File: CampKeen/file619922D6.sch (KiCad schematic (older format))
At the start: 40 parts

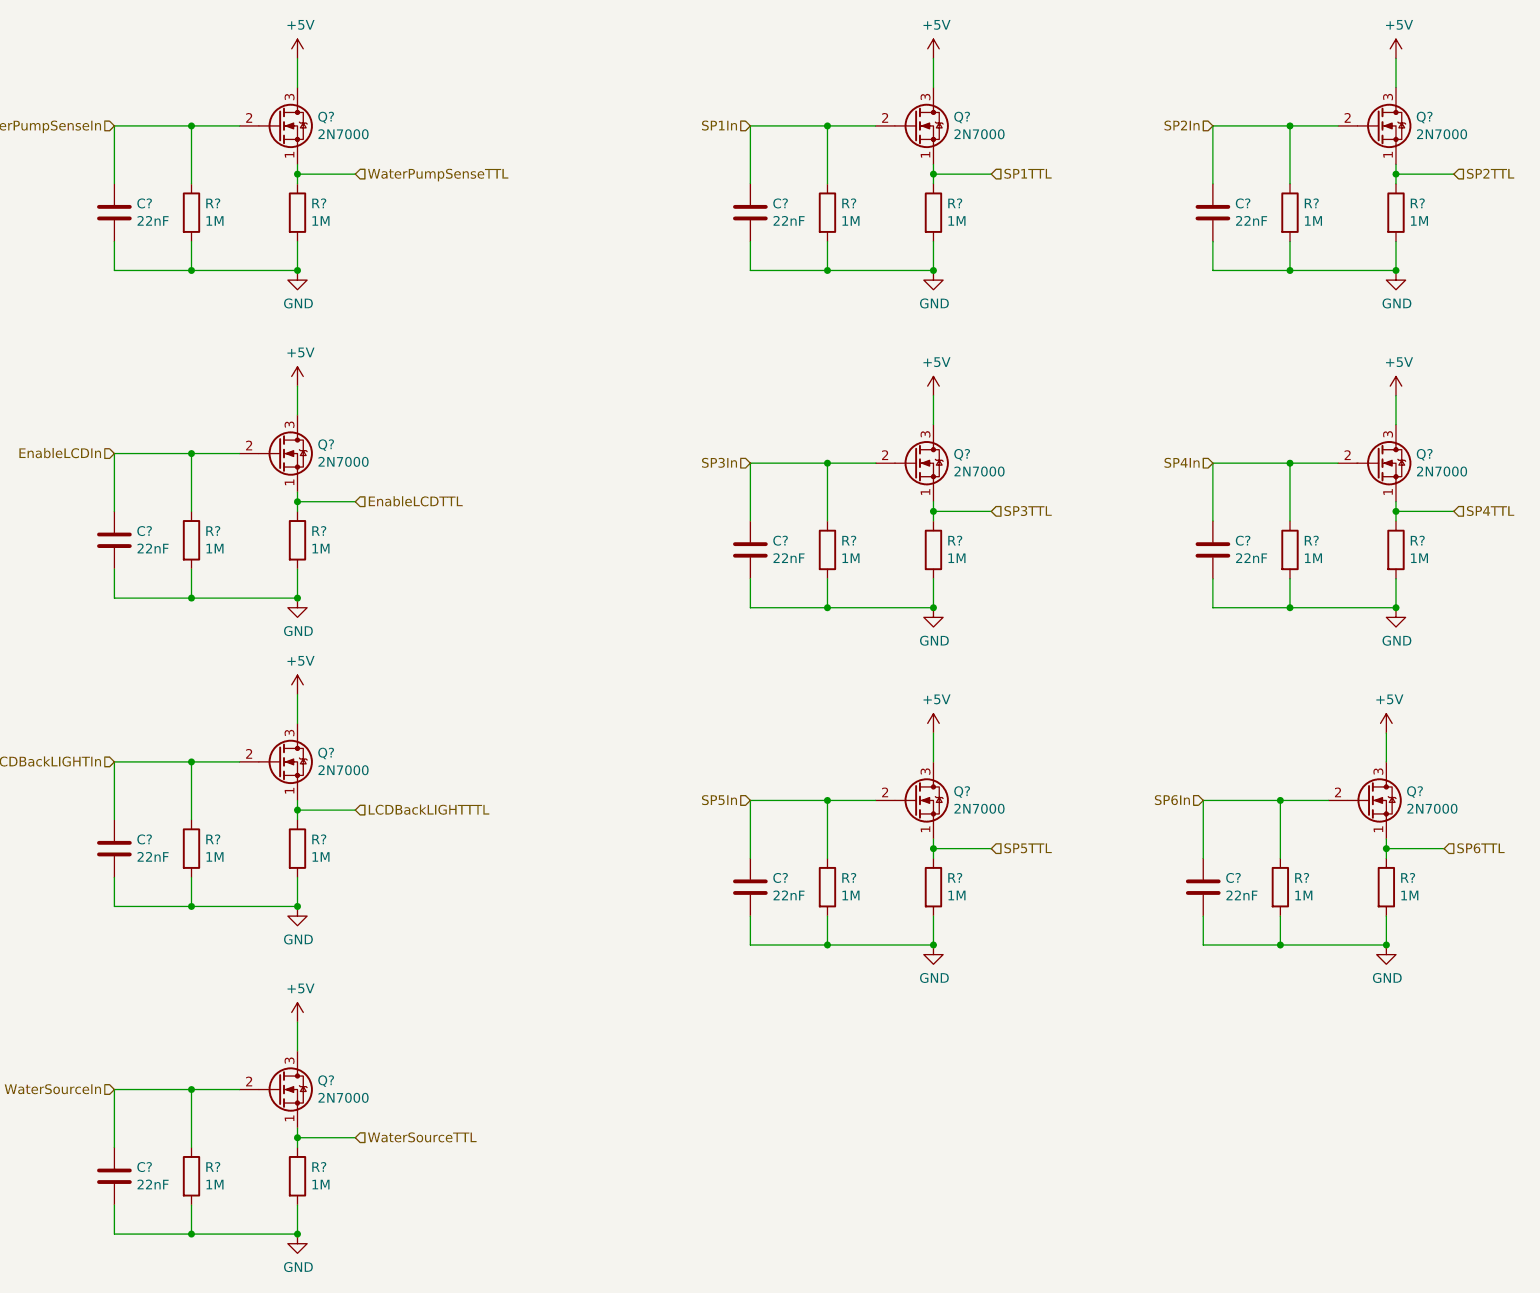
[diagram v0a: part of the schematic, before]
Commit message: updated the pin mapping to the terms. cleaned up the Schematic. PCB placement and routing is what is left to do.
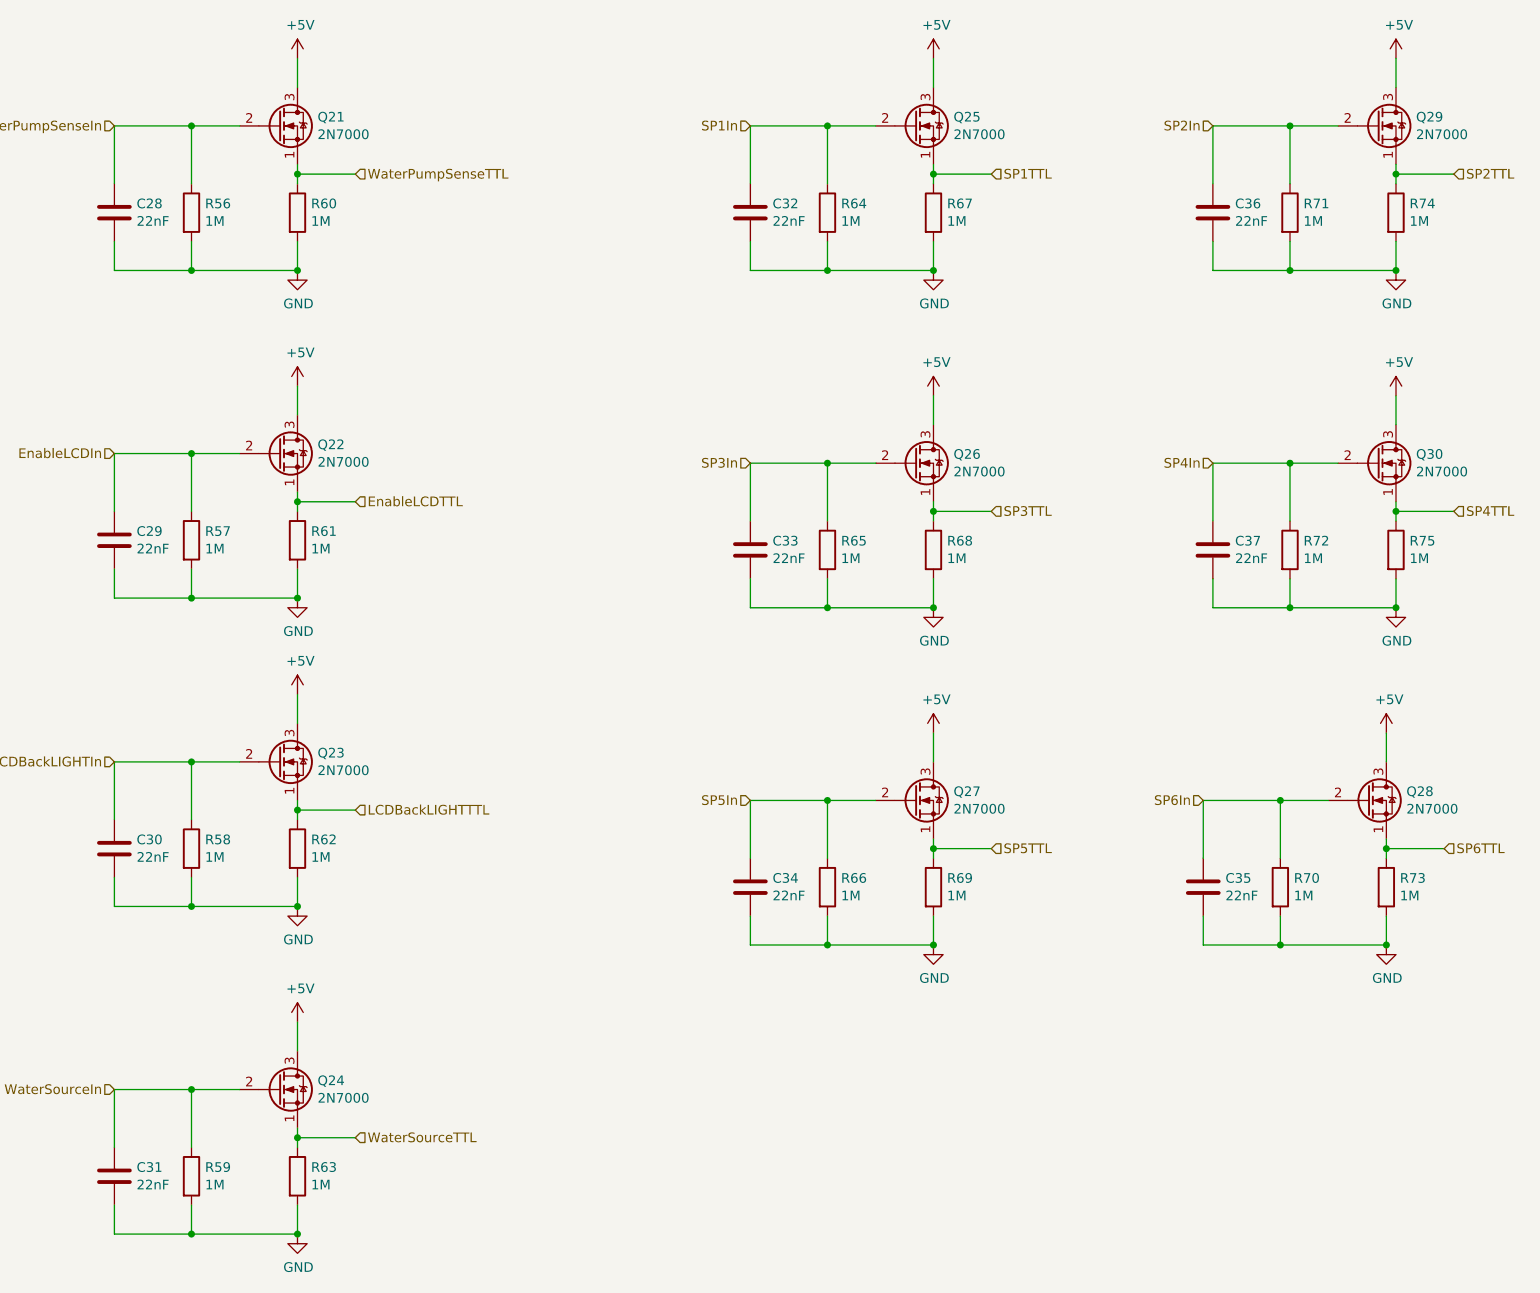
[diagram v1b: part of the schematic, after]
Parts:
- C28, C29, C30, C31, C32, C33, C34, C35, C36, C37: renamed from C?; footprint (none) -> Capacitor_THT:C_Disc_D4.7mm_W2.5mm_P5.00mm
- gave numbers to parts that had none: 30

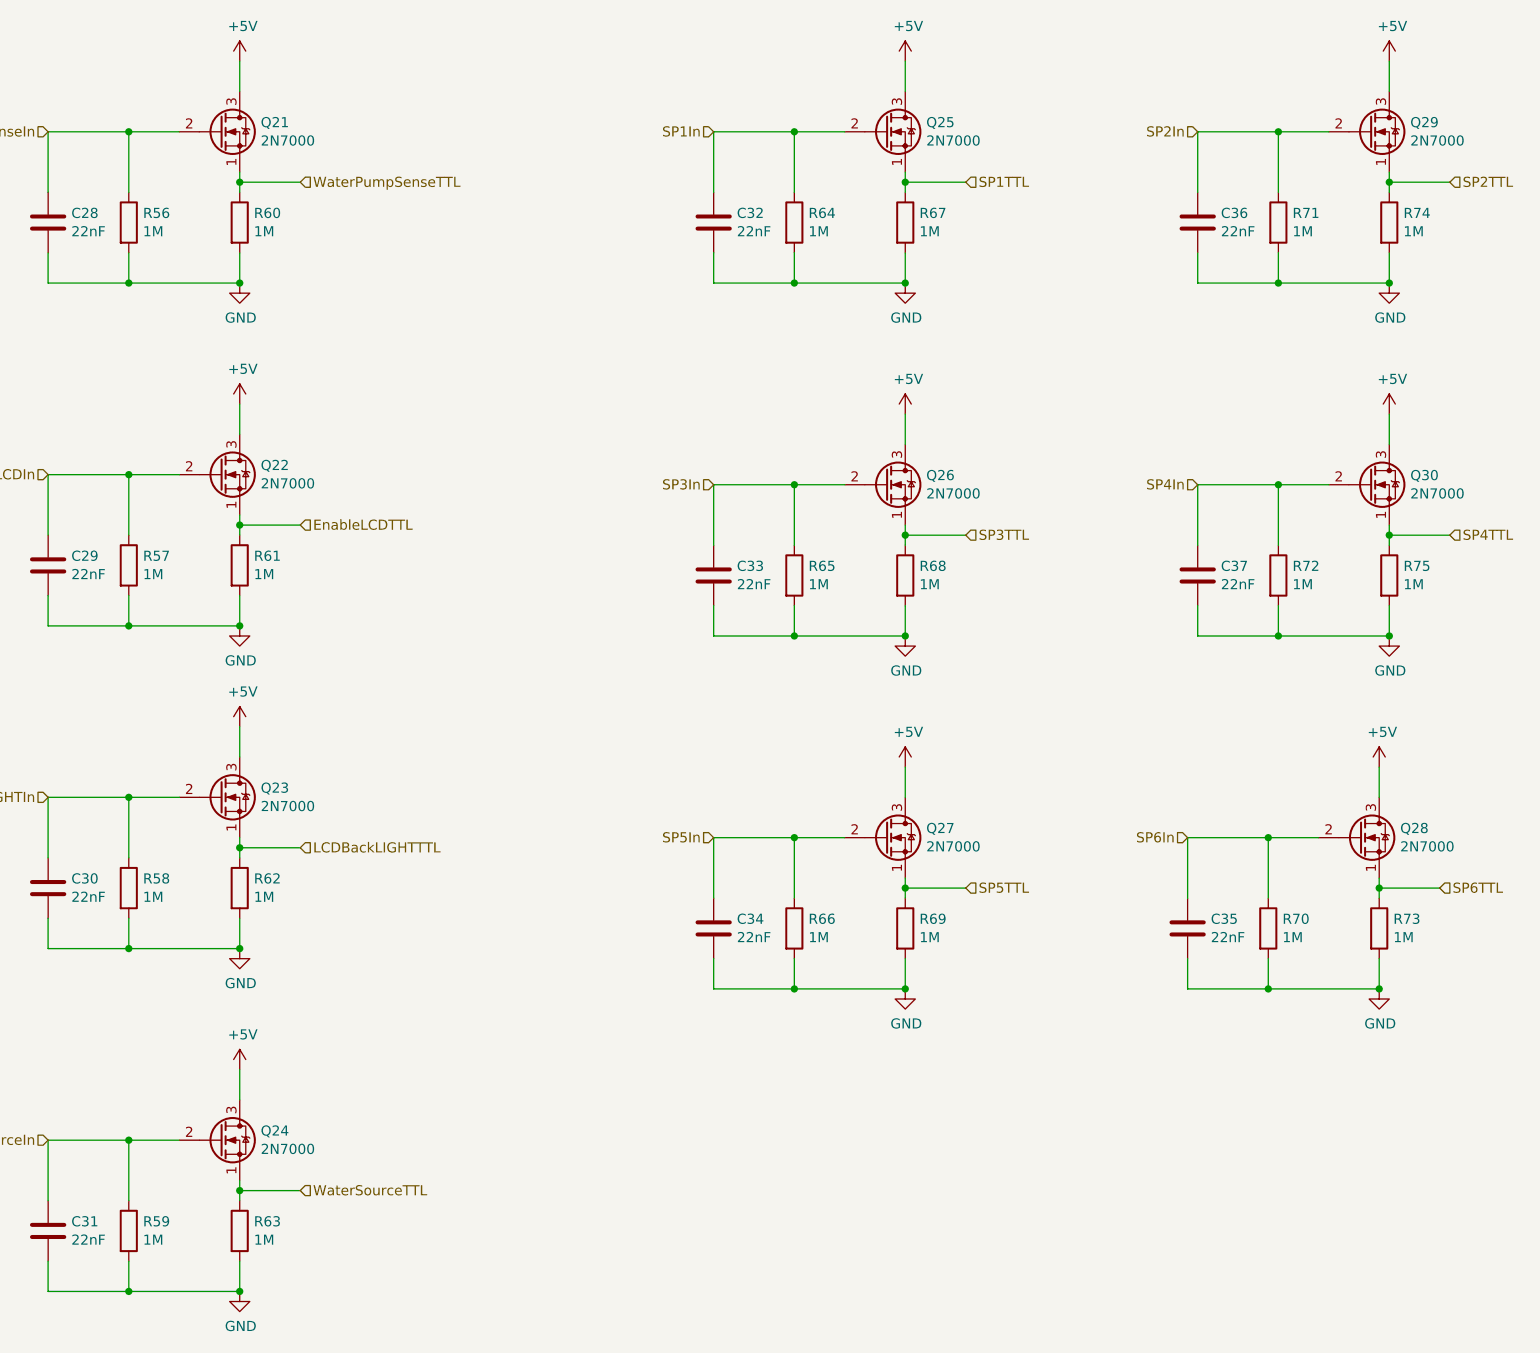
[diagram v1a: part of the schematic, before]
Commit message: separated the 12 and 5 volt outputs. added another spare output.
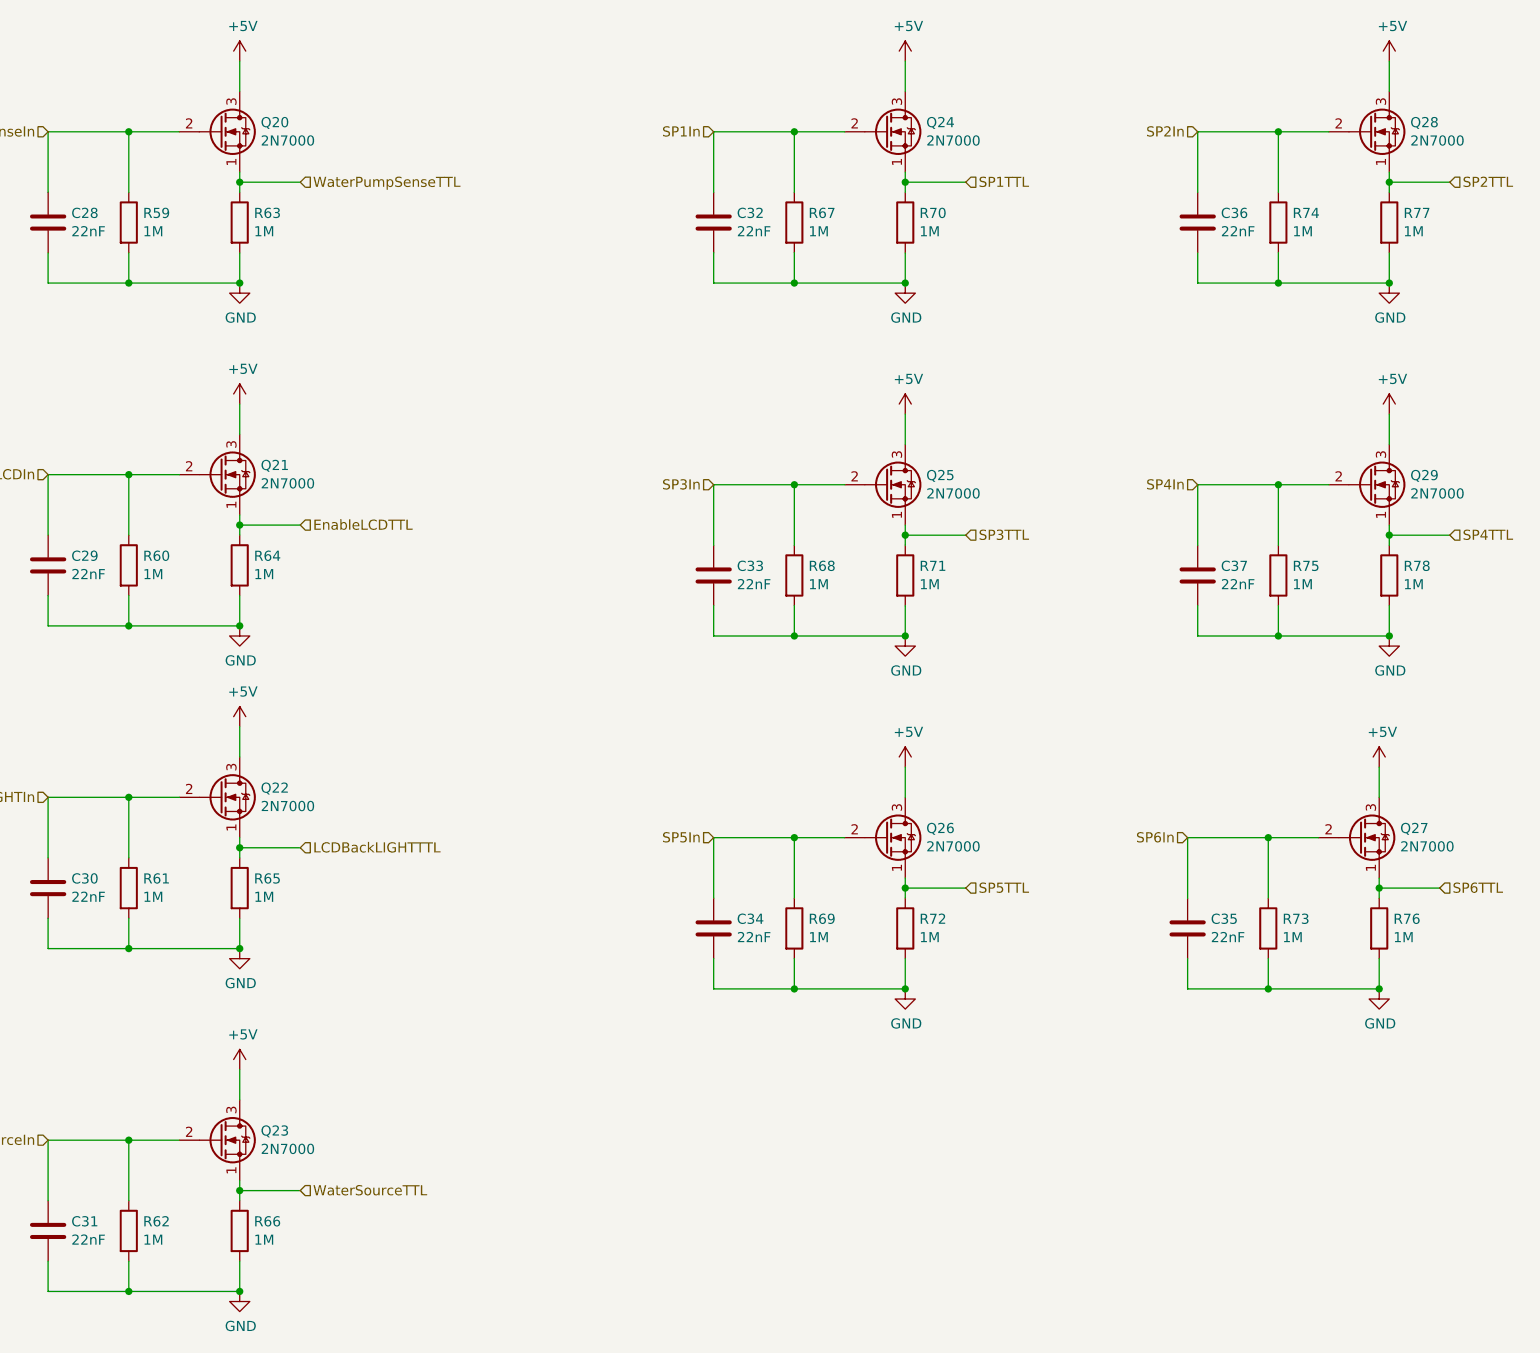
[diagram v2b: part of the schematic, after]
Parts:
- renumbered Q21 to Q20, Q22 to Q21, Q23 to Q22, Q24 to Q23, Q25 to Q24, Q26 to Q25, Q27 to Q26, Q28 to Q27, Q29 to Q28, Q30 to Q29, R56 to R59, R57 to R60, R58 to R61, R59 to R62, R60 to R63, R61 to R64, R62 to R65, R63 to R66, R64 to R67, R65 to R68, R66 to R69, R67 to R70, R68 to R71, R69 to R72, R70 to R73, R71 to R74, R72 to R75, R73 to R76, R74 to R77, R75 to R78
